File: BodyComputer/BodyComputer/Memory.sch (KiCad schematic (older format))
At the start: 24 parts, among them J1 MicroSD

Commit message: Update due to moving to another computer. Updated Schematic, Print-outs, PCB in development
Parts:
- gave numbers to parts that had none: 23
- renumbered J1 to J7
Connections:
- net FLASH_DATA_CLK: now also J8.5; no longer J8.6
- net FLASH_DATA_CMD: now also J8.6; no longer J8.5

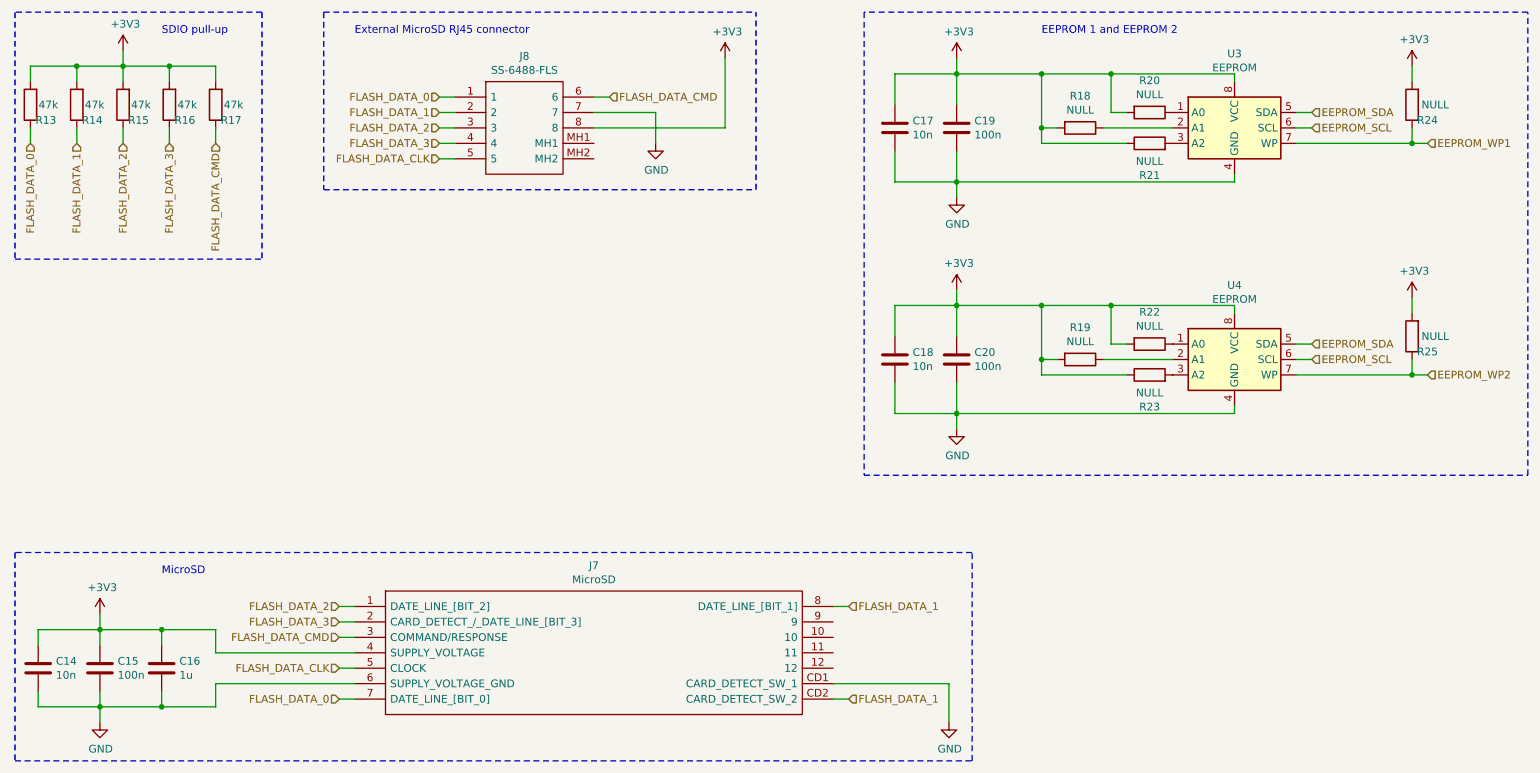
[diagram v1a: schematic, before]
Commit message: Updated schematic (DC/DC), 2-layer PCB
Updated schematic in multiple places, added elements, exchanged 3V3 stabilizer for a DC/DC converter. Nearly finished 2-layer PCB layout.
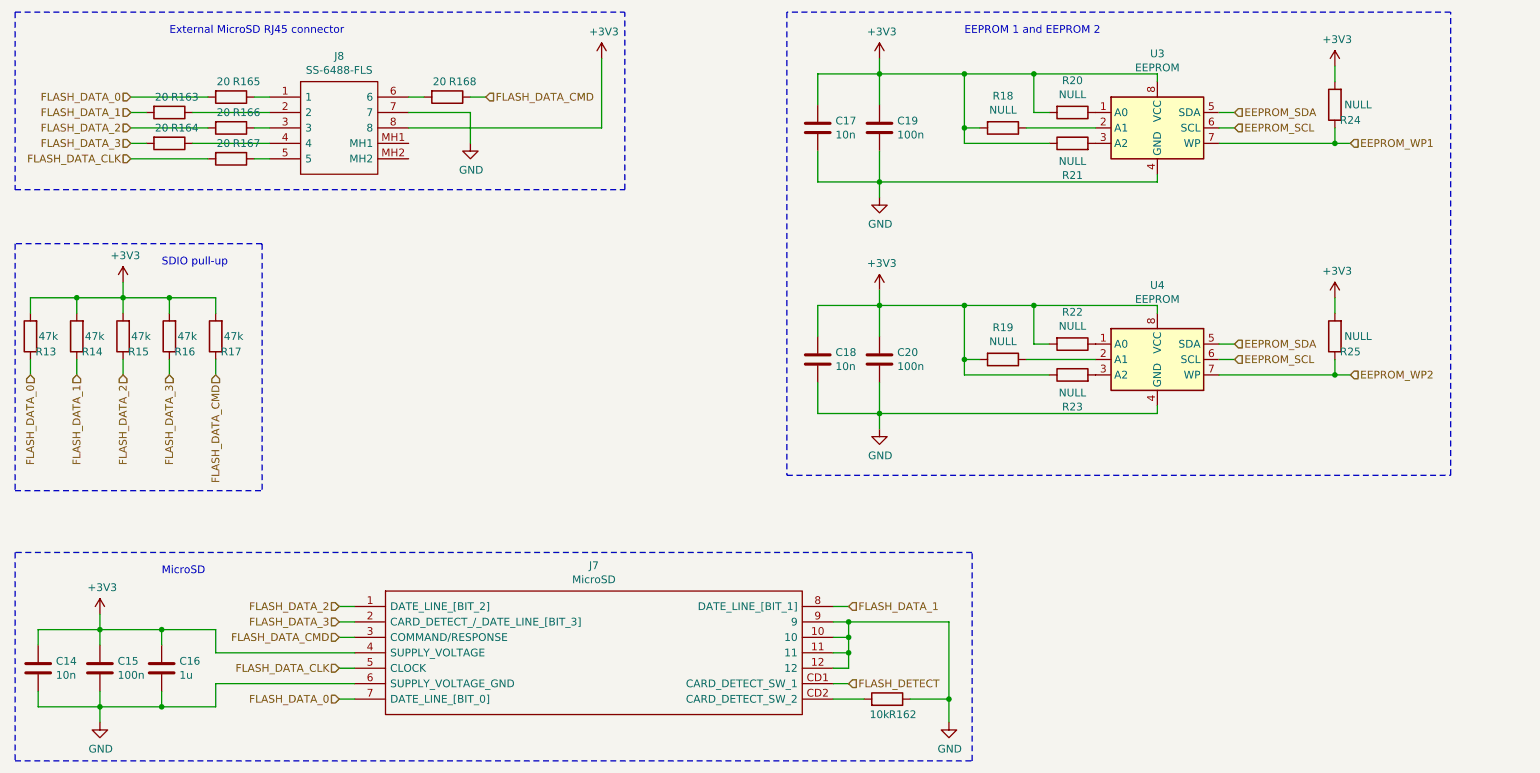
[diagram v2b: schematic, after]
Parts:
- added R162: 10k, Resistor_SMD:R_0603_1608Metric, symbol Device:R
- added R163, R164, R165, R166, R167, R168: 20, Resistor_SMD:R_0603_1608Metric, symbol Device:R
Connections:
- net FLASH_DATA_0: now also R165.2; no longer J8.1
- net FLASH_DATA_1: now also R163.2; no longer J7.CD2 (CARD_DETECT_SW_2), J8.2
- net FLASH_DATA_2: now also R166.2; no longer J8.3
- net FLASH_DATA_3: now also R164.2; no longer J8.4
- net FLASH_DATA_CLK: now also R167.2; no longer J8.5
- net FLASH_DATA_CMD: now also R168.1; no longer J8.6
- net GND: now also J7.10, J7.11, J7.12, J7.9, R162.1; no longer J7.CD1 (CARD_DETECT_SW_1)
- new net: J7.CD2 (CARD_DETECT_SW_2), R162.2
- new net: J8.1, R165.1
- new net: J8.2, R163.1
- new net: J8.3, R166.1
- new net: J8.4, R164.1
- new net: J8.5, R167.1
- new net: J8.6, R168.2
- new net FLASH_DETECT: J7.CD1 (CARD_DETECT_SW_1)
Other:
- moved on the sheet: C17, C18, C19, C20, J8, R13, R14, R15, R16, R17, R18, R19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
